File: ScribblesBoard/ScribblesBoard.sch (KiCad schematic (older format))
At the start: 28 parts, among them J1 Conn_01x04, J2 ICSP, J3 FTDI, J4 Bluetooth Connector 1, J5 Bluetooth Connector 2, J6 Battery Connection, U1 MIC5205-3.3, U2 BNO055, U3 ATMEGA328P-MU

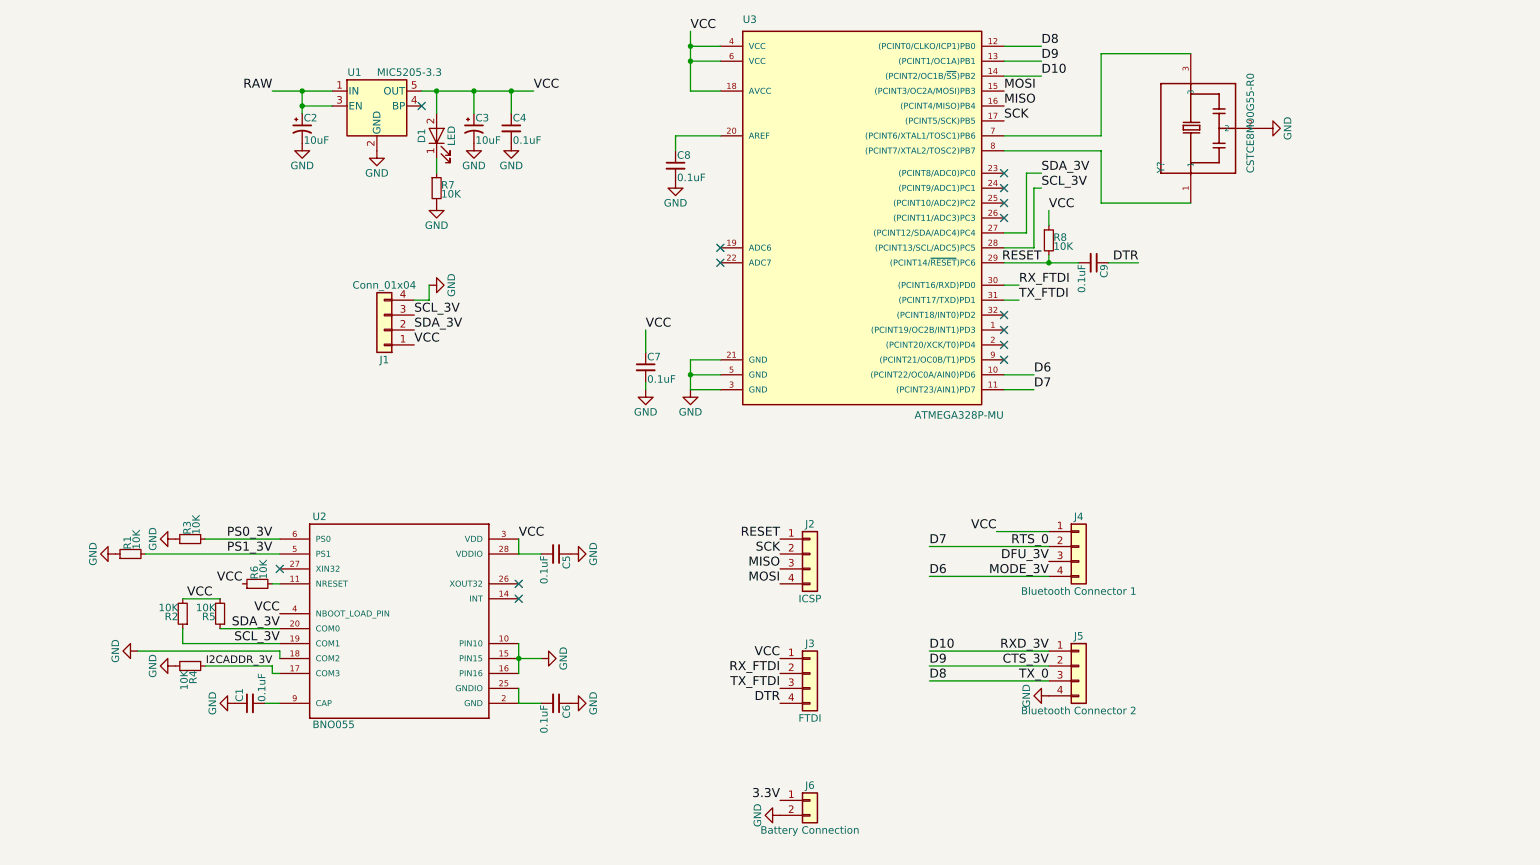
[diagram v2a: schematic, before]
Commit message: Added oscillator to imu
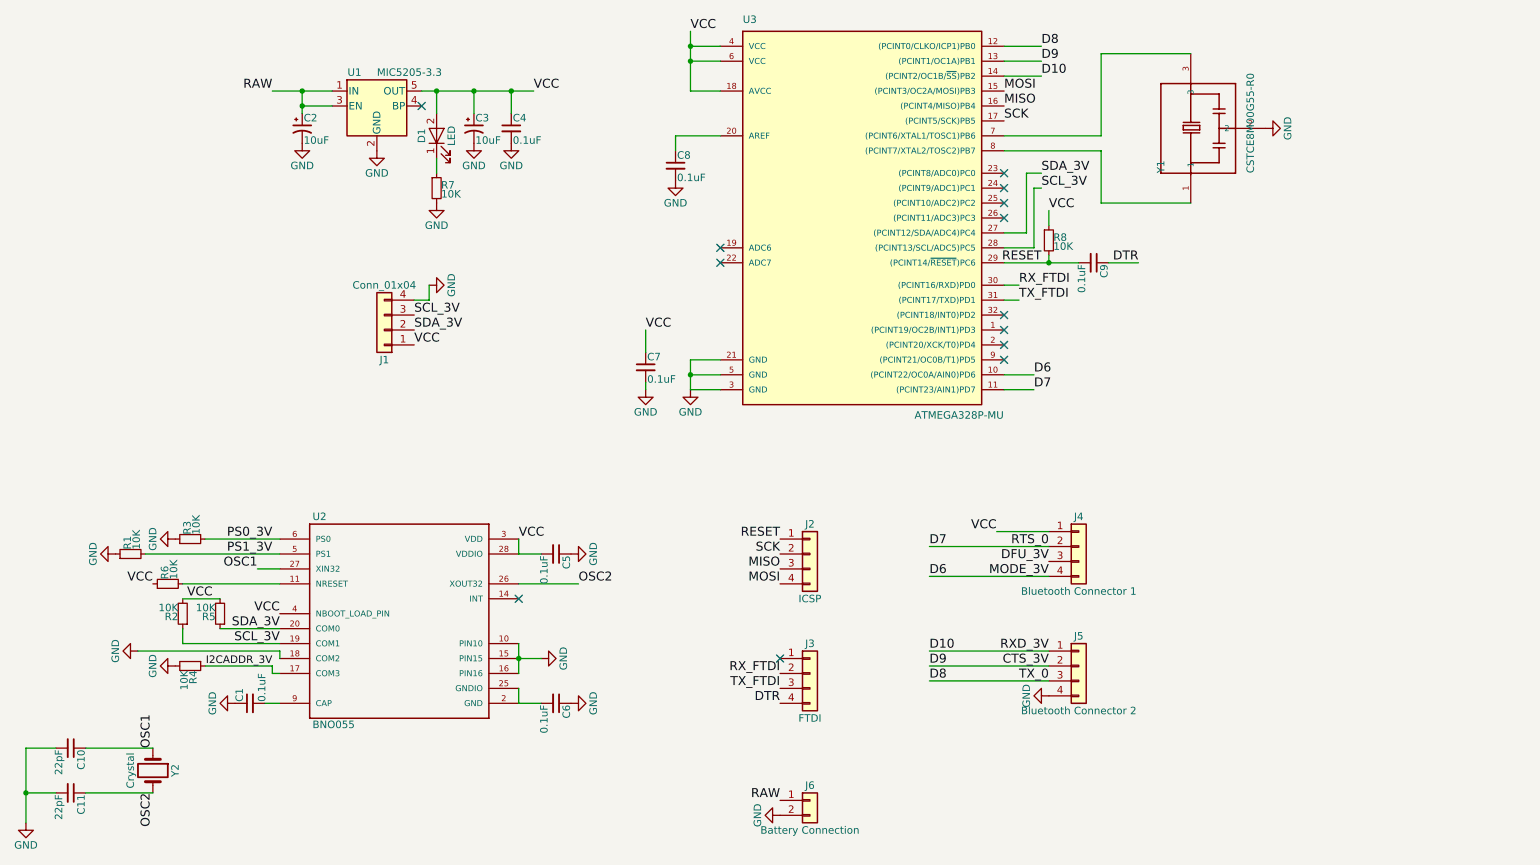
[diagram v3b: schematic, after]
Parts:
- added C10, C11: 22pF, Capacitors_SMD:C_0402, symbol C_Small
- added Y2: Crystal, lib_fp:ECS-.327-12.5-34B-TR, symbol Crystal
- Y1: renamed from Y?; footprint OSC_CSTCE8M00G55-R0 -> CSTCE8M00G55-R0:OSC_CSTCE8M00G55-R0
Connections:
- net 3.3V is gone; now on net RAW: J6.1 (Pin_1)
- net GND: now also C10.2, C11.2
- net VCC: no longer J3.1 (Pin_1)
- net OSC2: now reaches U2.26 (XOUT32)
- net OSC2: now also C11.1, Y2.2
- net OSC1: now reaches U2.27 (XIN32)
- net OSC1: now also C10.1, Y2.1
- no-connect marks 14 -> 13
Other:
- moved on the sheet: R6
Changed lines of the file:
@@
 Text Label 2400 4400 2    60   ~ 0
 PS1_3V
-NoConn ~ 2450 4500
-NoConn ~ 4050 4600
 NoConn ~ 4050 4700
 $Comp
@@
 L R_Small R6
 U 1 1 5A80E8AA
-P 2300 4600
-F 0 "R6" H 2330 4620 50  0000 L CNN
-F 1 "10K" H 2330 4560 50  0000 L CNN
-F 2 "Resistors_SMD:R_0402" H 2300 4600 50  0001 C CNN
-F 3 "" H 2300 4600 50  0001 C CNN
-	1    2300 4600
+P 1700 4600
+F 0 "R6" H 1730 4620 50  0000 L CNN
+F 1 "10K" H 1730 4560 50  0000 L CNN
+F 2 "Resistors_SMD:R_0402" H 1700 4600 50  0001 C CNN
+F 3 "" H 1700 4600 50  0001 C CNN
+	1    1700 4600
 	0    -1   -1   0
 $EndComp
-Text Label 2200 4600 2    60   ~ 0
+Text Label 1600 4600 2    60   ~ 0
 VCC
 Text Label 7300 1400 0    60   ~ 0
@@
 	2450 5050 1500 5050
 Wire Wire Line
-	2450 4600 2400 4600
+	1800 4600 2450 4600
 Wire Wire Line
 	7600 2450 7600 2400
@@
 Text Label 5800 5200 2    60   ~ 0
 RX_FTDI
-Text Label 5800 5100 2    60   ~ 0
-VCC
 Wire Wire Line
 	7300 2600 7400 2600
@@
 	1    0    0    -1
 $EndComp
-Text Label 5800 6050 2    60   ~ 0
-3.3V
 $Comp
 L GND #PWR019
@@
 $EndComp
 $Comp
-L CSTCE8M00G55-R0 Y?
+L CSTCE8M00G55-R0 Y1
 U 1 1 5A9B4668
 P 8650 1550
-F 0 "Y?" H 8350 1850 50  0000 L CNN
+F 0 "Y1" H 8350 1850 50  0000 L CNN
 F 1 "CSTCE8M00G55-R0" H 8350 1250 50  0000 L CNN
-F 2 "OSC_CSTCE8M00G55-R0" H 8650 1550 50  0001 L CNN
+F 2 "CSTCE8M00G55-R0:OSC_CSTCE8M00G55-R0" H 8650 1550 50  0001 L CNN
 F 3 "muRata" H 8650 1550 50  0001 L CNN
 	1    8650 1550
@@
 Wire Wire Line
 	7950 1050 8550 1050
+Text Label 5800 6050 2    60   ~ 0
+RAW
+NoConn ~ 5800 5100
+$Comp
+L Crystal Y2
+U 1 1 5A9B8A12
+P 1600 5850
+F 0 "Y2" H 1600 6000 50  0000 C CNN
+F 1 "Crystal" H 1600 5700 50  0000 C CNN
+F 2 "lib_fp:ECS-.327-12.5-34B-TR" H 1600 5850 50  0001 C CNN
+F 3 "" H 1600 5850 50  0001 C CNN
+	1    1600 5850
+	0    1    1    0
+$EndComp
+$Comp
+L C_Small C10
+U 1 1 5A9B8BC1
+P 1050 5700
+F 0 "C10" H 1060 5770 50  0000 L CNN
+F 1 "22pF" H 1060 5620 50  0000 L CNN
+F 2 "Capacitors_SMD:C_0402" H 1050 5700 50  0001 C CNN
+F 3 "" H 1050 5700 50  0001 C CNN
+	1    1050 5700
+	0    1    1    0
+$EndComp
+$Comp
+L C_Small C11
+U 1 1 5A9B8CF0
+P 1050 6000
+F 0 "C11" H 1060 6070 50  0000 L CNN
+F 1 "22pF" H 1060 5920 50  0000 L CNN
+F 2 "Capacitors_SMD:C_0402" H 1050 6000 50  0001 C CNN
+F 3 "" H 1050 6000 50  0001 C CNN
+	1    1050 6000
+	0    1    1    0
+$EndComp
+Wire Wire Line
+	2450 4500 2300 4500
+Text Label 2300 4500 2    60   ~ 0
+OSC1
+Text Label 4450 4600 0    60   ~ 0
+OSC2
+Wire Wire Line
+	4050 4600 4450 4600
+Text Label 1600 6000 3    60   ~ 0
+OSC2
+Text Label 1600 5700 1    60   ~ 0
+OSC1
+Wire Wire Line
+	1600 5700 1150 5700
+Wire Wire Line
+	1600 6000 1150 6000
+Wire Wire Line
+	950  5700 750  5700
+Wire Wire Line
+	750  5700 750  6200
+Wire Wire Line
+	750  6000 950  6000
+Connection ~ 750  6000
+$Comp
+L GND #PWR021
+U 1 1 5A9B986E
+P 750 6200
+F 0 "#PWR021" H 750 5950 50  0001 C CNN
+F 1 "GND" H 750 6050 50  0000 C CNN
+F 2 "" H 750 6200 50  0001 C CNN
+F 3 "" H 750 6200 50  0001 C CNN
+	1    750  6200
+	1    0    0    -1
+$EndComp
 $EndSCHEMATC
